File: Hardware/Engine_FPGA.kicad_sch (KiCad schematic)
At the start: 8 parts, among them J12 Conn_02x05_Odd_Even, SW1 SW_KJ06RTT, U2 AT40K20-2EQJ

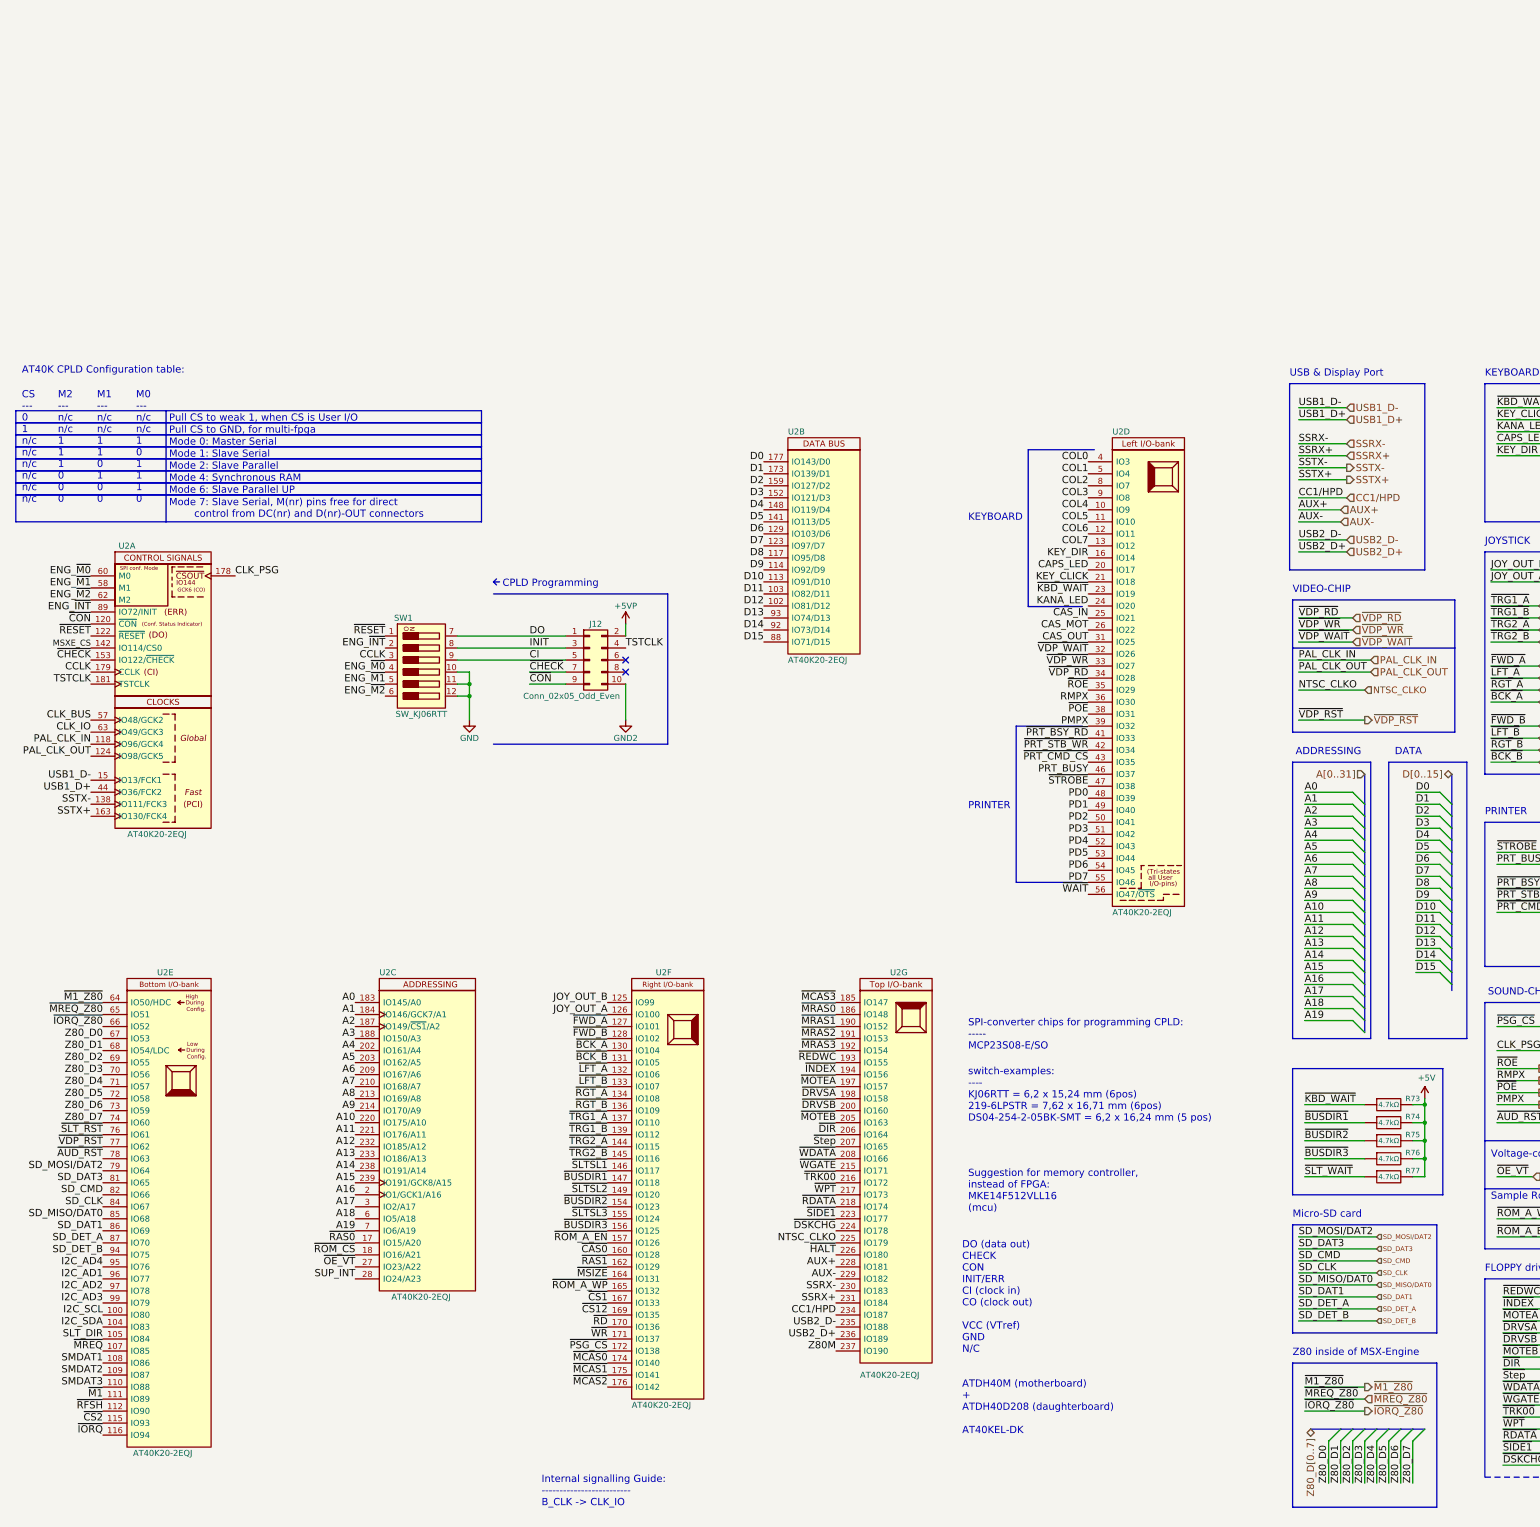
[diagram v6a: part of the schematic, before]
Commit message: Multiple redesigns of the IO-shield. Replaced FPGA with lower pin-count AT10K, since the higher pin-count one is now obsolete.
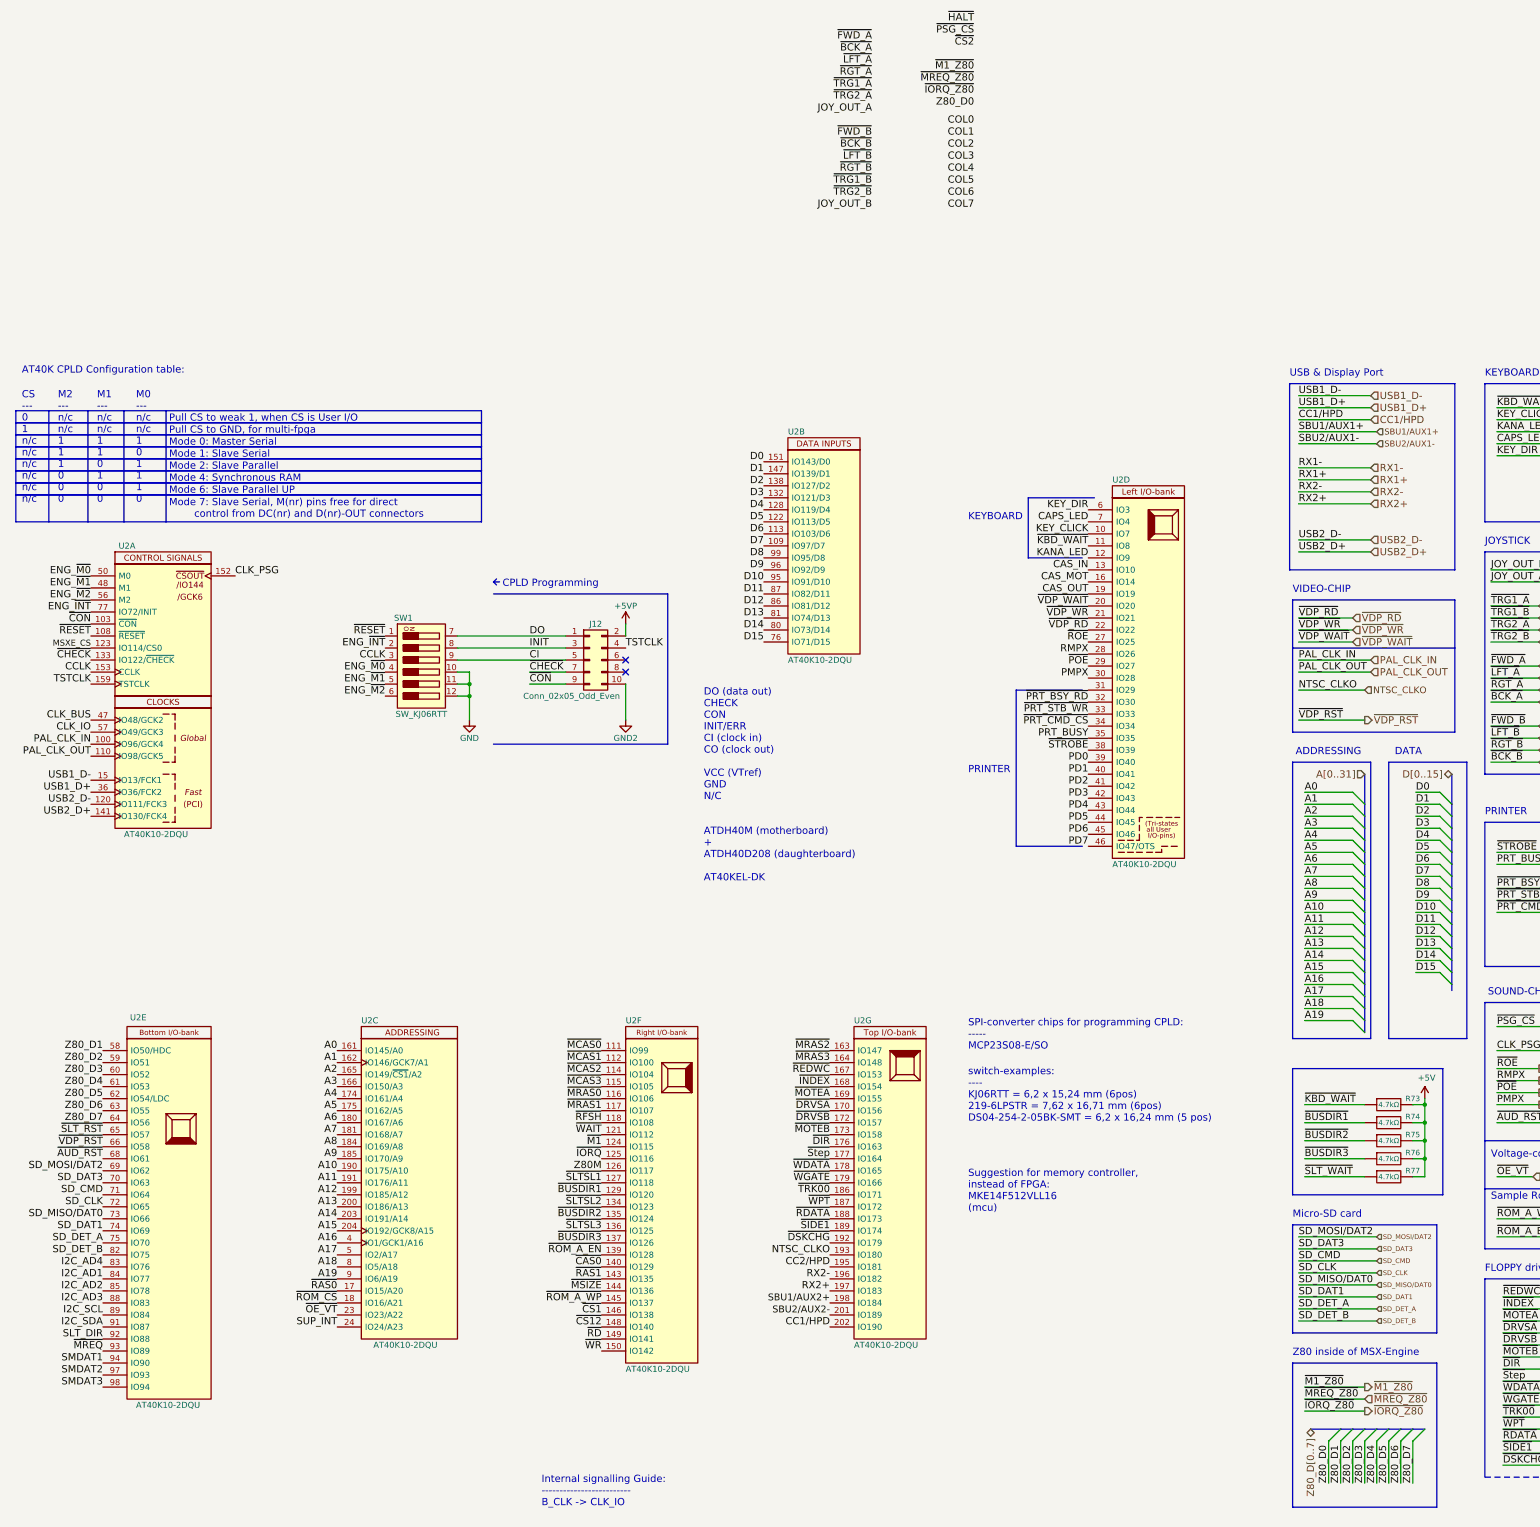
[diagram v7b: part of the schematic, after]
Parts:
- U2: value AT40K20-2EQJ -> AT40K10-2DQU; footprint Package_QFP:PQFP-240_32.1x32.1mm_P0.5mm -> Package_QFP:PQFP-208_28x28mm_P0.5mm; symbol LRJ-parts:AT40K20-2EQJ -> LRJ-parts:AT40K10-2DQU; MPN AT40K20-2EQJ -> AT40K10-2DQU; Manufacturer (none) -> Microchip/ATmel; Manufacturer_Name Microchip -> (none); Status (none) -> Active
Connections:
- net A0: now also U2.161 (IO145/A0); no longer U2.183 (IO145/A0)
- net A1: now also U2.162 (IO146/GCK7/A1); no longer U2.184 (IO146/GCK7/A1)
- net A10: now also U2.190 (IO175/A10); no longer U2.220 (IO175/A10)
- net A11: now also U2.191 (IO176/A11); no longer U2.221 (IO176/A11)
- net A12: now also U2.199 (IO185/A12); no longer U2.232 (IO185/A12)
- net A13: now also U2.200 (IO186/A13); no longer U2.233 (IO186/A13)
- net A14: now also U2.203 (IO191/A14); no longer U2.238 (IO191/A14)
- net A15: now also U2.204 (IO192/GCK8/A15); no longer U2.239 (IO191/GCK8/A15)
- net A16: now also U2.4 (IO1/GCK1/A16); no longer U2.2 (IO1/GCK1/A16)
- net A17: now also U2.5 (IO2/A17); no longer U2.3 (IO2/A17)
- net A18: now also U2.8 (IO5/A18); no longer U2.6 (IO5/A18)
- net A19: now also U2.9 (IO6/A19); no longer U2.7 (IO6/A19)
- net A2: now also U2.165 (IO149/~{CS1}/A2); no longer U2.187 (IO149/~{CS1}/A2)
- net A3: now also U2.166 (IO150/A3); no longer U2.188 (IO150/A3)
- net A4: now also U2.174 (IO161/A4); no longer U2.202 (IO161/A4)
- net A5: now also U2.175 (IO162/A5); no longer U2.203 (IO162/A5)
- net A6: now also U2.180 (IO167/A6); no longer U2.209 (IO167/A6)
- net A7: now also U2.181 (IO168/A7); no longer U2.210 (IO168/A7)
- net A8: now also U2.184 (IO169/A8); no longer U2.213 (IO169/A8)
- net A9: now also U2.185 (IO170/A9); no longer U2.214 (IO170/A9)
- net CAPS_LED: now also U2.7 (IO4); no longer U2.20 (IO17)
- net CAS_IN: now also U2.13 (IO10); no longer U2.25 (IO21)
- net CAS_MOT: now also U2.16 (IO14); no longer U2.26 (IO22)
- net CAS_OUT: now also U2.19 (IO19); no longer U2.31 (IO25)
- net CC1/HPD: now also U2.202 (IO190); no longer U2.234 (IO187)
- net CCLK: now also U2.153 (CCLK); no longer U2.179 (CCLK)
- net CLK_BUS: now also U2.47 (IO48/GCK2); no longer U2.57 (IO48/GCK2)
- net CLK_IO: now also U2.57 (IO49/GCK3); no longer U2.63 (IO49/GCK3)
- net CLK_PSG: now also U2.152 (IO144/GCK6/~{CSOUT}); no longer U2.178 (IO144/GCK6/~{CSOUT})
- net COL0: no longer U2.4 (IO3)
- net COL1: no longer U2.5 (IO4)
- net COL2: no longer U2.8 (IO7)
- net COL3: no longer U2.9 (IO8)
- net COL4: no longer U2.10 (IO9)
- net COL5: no longer U2.11 (IO10)
- net COL6: no longer U2.12 (IO11)
- net COL7: no longer U2.13 (IO12)
- net D0: now also U2.151 (IO143/D0); no longer U2.177 (IO143/D0)
- net D1: now also U2.147 (IO139/D1); no longer U2.173 (IO139/D1)
- net D10: now also U2.95 (IO91/D10); no longer U2.113 (IO91/D10)
- net D11: now also U2.87 (IO82/D11); no longer U2.103 (IO82/D11)
- net D12: now also U2.86 (IO81/D12); no longer U2.102 (IO81/D12)
- net D13: now also U2.81 (IO74/D13); no longer U2.93 (IO74/D13)
- net D14: now also U2.80 (IO73/D14); no longer U2.92 (IO73/D14)
- net D15: now also U2.76 (IO71/D15); no longer U2.88 (IO71/D15)
- net D2: now also U2.138 (IO127/D2); no longer U2.159 (IO127/D2)
- net D3: now also U2.132 (IO121/D3); no longer U2.152 (IO121/D3)
- net D4: now also U2.128 (IO119/D4); no longer U2.148 (IO119/D4)
- net D5: now also U2.122 (IO113/D5); no longer U2.141 (IO113/D5)
- net D6: now also U2.113 (IO103/D6); no longer U2.129 (IO103/D6)
- net D7: now also U2.109 (IO97/D7); no longer U2.123 (IO97/D7)
- net D8: now also U2.99 (IO95/D8); no longer U2.117 (IO95/D8)
- net D9: now also U2.96 (IO92/D9); no longer U2.114 (IO92/D9)
- net ENG_~{INT}: now also U2.77 (IO72/INIT); no longer U2.89 (IO72/INIT)
- net ENG_~{M0}: now also U2.50 (M0); no longer U2.60 (M0)
- net ENG_~{M1}: now also U2.48 (M1); no longer U2.58 (M1)
- net ENG_~{M2}: now also U2.56 (M2); no longer U2.62 (M2)
- net I2C_AD1: now also U2.84 (IO77); no longer U2.96 (IO77)
- net I2C_AD2: now also U2.85 (IO78); no longer U2.97 (IO78)
- net I2C_AD3: now also U2.88 (IO83); no longer U2.99 (IO79)
- net I2C_AD4: now also U2.83 (IO76); no longer U2.95 (IO76)
- net I2C_SCL: now also U2.89 (IO84); no longer U2.100 (IO80)
- net I2C_SDA: now also U2.91 (IO87); no longer U2.104 (IO83)
- net JOY_OUT_A: no longer U2.126 (IO100)
- net JOY_OUT_B: no longer U2.125 (IO99)
- net KANA_LED: now also U2.12 (IO9); no longer U2.24 (IO20)
- net KEY_CLICK: now also U2.10 (IO7); no longer U2.21 (IO18)
- net KEY_DIR: now also U2.6 (IO3); no longer U2.16 (IO14)
- net MSXE_CS: now also U2.123 (IO114/CS0); no longer U2.142 (IO114/CS0)
- net NTSC_CLKO: now also U2.193 (IO180); no longer U2.225 (IO179)
- net PAL_CLK_IN: now also U2.100 (IO96/GCK4); no longer U2.118 (IO96/GCK4)
- net PAL_CLK_OUT: now also U2.110 (IO98/GCK5); no longer U2.124 (IO98/GCK5)
- net PD0: now also U2.39 (IO40); no longer U2.48 (IO39)
- net PD1: now also U2.40 (IO41); no longer U2.49 (IO40)
- net PD2: now also U2.41 (IO42); no longer U2.50 (IO41)
- net PD3: now also U2.42 (IO43); no longer U2.51 (IO42)
- net PD4: now also U2.43 (IO44); no longer U2.52 (IO43)
- net PD5: now also U2.44 (IO45); no longer U2.53 (IO44)
- net PD6: now also U2.45 (IO46); no longer U2.54 (IO45)
- net PD7: now also U2.46 (IO47/OTS); no longer U2.55 (IO46)
- net PMPX: now also U2.30 (IO28); no longer U2.39 (IO32)
- net PRT_BUSY: now also U2.35 (IO35); no longer U2.46 (IO37)
- net RMPX: now also U2.28 (IO26); no longer U2.36 (IO30)
- net SD_CLK: now also U2.72 (IO65); no longer U2.84 (IO67)
- net SD_CMD: now also U2.71 (IO64); no longer U2.82 (IO66)
- net SD_DAT1: now also U2.74 (IO69); no longer U2.86 (IO69)
- net SD_DAT3: now also U2.70 (IO63); no longer U2.81 (IO65)
- net SD_DET_A: now also U2.75 (IO70); no longer U2.87 (IO70)
- net SD_DET_B: now also U2.82 (IO75); no longer U2.94 (IO75)
- net SD_MISO/DAT0: now also U2.73 (IO66); no longer U2.85 (IO68)
- net SD_MOSI/DAT2: now also U2.69 (IO62); no longer U2.79 (IO64)
- net SLT_DIR: now also U2.92 (IO88); no longer U2.105 (IO84)
- net SMDAT1: now also U2.94 (IO90); no longer U2.108 (IO86)
- net SMDAT2: now also U2.97 (IO93); no longer U2.109 (IO87)
- net SMDAT3: now also U2.98 (IO94); no longer U2.110 (IO88)
- net SUP_INT: now also U2.24 (IO24/A23); no longer U2.28 (IO24/A23)
- net TSTCLK: now also U2.159 (TSTCLK); no longer U2.181 (TSTCLK)
- net USB1_D+: now also U2.36 (IO36/FCK2); no longer U2.44 (IO36/FCK2)
- net USB2_D+: now also U2.141 (IO130/FCK4); no longer U2.236 (IO189)
- net USB2_D-: now also U2.120 (IO111/FCK3); no longer U2.235 (IO188)
- net Z80M: now also U2.126 (IO117); no longer U2.237 (IO190)
- net Z80_D0: no longer U2.67 (IO53)
- net Z80_D1: now also U2.58 (IO50/HDC); no longer U2.68 (IO54/LDC)
- net Z80_D2: now also U2.59 (IO51); no longer U2.69 (IO55)
- net Z80_D3: now also U2.60 (IO52); no longer U2.70 (IO56)
- net Z80_D4: now also U2.61 (IO53); no longer U2.71 (IO57)
- net Z80_D5: now also U2.62 (IO54/LDC); no longer U2.72 (IO58)
- net Z80_D6: now also U2.63 (IO55); no longer U2.73 (IO59)
- net Z80_D7: now also U2.64 (IO56); no longer U2.74 (IO60)
- net ~{AUD_RST}: now also U2.68 (IO61); no longer U2.78 (IO63)
- net ~{BCK_A}: no longer U2.130 (IO104)
- net ~{BCK_B}: no longer U2.131 (IO105)
- net ~{BUSDIR1}: now also U2.129 (IO120); no longer U2.147 (IO118)
- net ~{BUSDIR2}: now also U2.135 (IO124); no longer U2.154 (IO123)
- net ~{BUSDIR3}: now also U2.137 (IO126); no longer U2.156 (IO125)
- net ~{CAS0}: now also U2.140 (IO129); no longer U2.160 (IO128)
- net ~{CHECK}: now also U2.133 (IO122/~{CHECK}); no longer U2.153 (IO122/~{CHECK})
- net ~{CON}: now also U2.103 (~{CON}); no longer U2.120 (~{CON})
- net ~{CS12}: now also U2.148 (IO140); no longer U2.169 (IO135)
- net ~{CS1}: now also U2.146 (IO138); no longer U2.167 (IO133)
- net ~{CS2}: no longer U2.115 (IO93)
- net ~{DIR}: now also U2.176 (IO163); no longer U2.206 (IO164)
- net ~{DRVSA}: now also U2.170 (IO156); no longer U2.198 (IO158)
- net ~{DRVSB}: now also U2.172 (IO157); no longer U2.200 (IO160)
- net ~{DSKCHG}: now also U2.192 (IO179); no longer U2.224 (IO178)
- net ~{FWD_A}: no longer U2.127 (IO101)
- net ~{FWD_B}: no longer U2.128 (IO102)
- net ~{HALT}: no longer U2.226 (IO180)
- net ~{INDEX}: now also U2.168 (IO154); no longer U2.194 (IO156)
- net ~{IORQ_Z80}: no longer U2.66 (IO52)
- net ~{IORQ}: now also U2.125 (IO116); no longer U2.116 (IO94)
- net ~{KBD_WAIT}: now also U2.11 (IO8); no longer U2.23 (IO19)
- net ~{LFT_A}: no longer U2.132 (IO106)
- net ~{LFT_B}: no longer U2.133 (IO107)
- net ~{M1_Z80}: no longer U2.64 (IO50/HDC)
- net ~{M1}: now also U2.124 (IO115); no longer U2.111 (IO89)
- net ~{MCAS0}: now also U2.111 (IO99); no longer U2.174 (IO140)
- net ~{MCAS1}: now also U2.112 (IO100); no longer U2.175 (IO141)
- net ~{MCAS2}: now also U2.114 (IO104); no longer U2.176 (IO142)
- net ~{MCAS3}: now also U2.115 (IO105); no longer U2.185 (IO147)
- net ~{MOTEA}: now also U2.169 (IO155); no longer U2.197 (IO157)
- net ~{MOTEB}: now also U2.173 (IO158); no longer U2.205 (IO163)
- net ~{MRAS0}: now also U2.116 (IO106); no longer U2.186 (IO148)
- net ~{MRAS1}: now also U2.117 (IO107); no longer U2.190 (IO152)
- net ~{MRAS2}: now also U2.163 (IO147); no longer U2.191 (IO153)
- net ~{MRAS3}: now also U2.164 (IO148); no longer U2.192 (IO154)
- net ~{MREQ_Z80}: no longer U2.65 (IO51)
- net ~{MREQ}: now also U2.93 (IO89); no longer U2.107 (IO85)
- net ~{MSIZE}: now also U2.144 (IO136); no longer U2.164 (IO131)
- net ~{OE_VT}: now also U2.23 (IO23/A22); no longer U2.27 (IO23/A22)
- net ~{POE}: now also U2.29 (IO27); no longer U2.38 (IO31)
- net ~{PRT_BSY_RD}: now also U2.32 (IO30); no longer U2.41 (IO33)
- net ~{PRT_CMD_CS}: now also U2.34 (IO34); no longer U2.43 (IO35)
- net ~{PRT_STB_WR}: now also U2.33 (IO33); no longer U2.42 (IO34)
- net ~{PSG_CS}: no longer U2.172 (IO138)
- net ~{RAS1}: now also U2.143 (IO135); no longer U2.162 (IO129)
- net ~{RDATA}: now also U2.188 (IO173); no longer U2.218 (IO174)
- net ~{RD}: now also U2.149 (IO141); no longer U2.170 (IO136)
- net ~{REDWC}: now also U2.167 (IO153); no longer U2.193 (IO155)
- net ~{RESET}: now also U2.108 (~{RESET}); no longer U2.122 (~{RESET})
- net ~{RFSH}: now also U2.118 (IO108); no longer U2.112 (IO90)
- net ~{RGT_A}: no longer U2.134 (IO108)
- net ~{RGT_B}: no longer U2.136 (IO109)
- net ~{ROE}: now also U2.27 (IO25); no longer U2.35 (IO29)
- net ~{ROM_A_EN}: now also U2.139 (IO128); no longer U2.157 (IO126)
- net ~{ROM_A_WP}: now also U2.145 (IO137); no longer U2.165 (IO132)
- net ~{SIDE1}: now also U2.189 (IO174); no longer U2.223 (IO177)
- net ~{SLTSL1}: now also U2.127 (IO118); no longer U2.146 (IO117)
- net ~{SLTSL2}: now also U2.134 (IO123); no longer U2.149 (IO120)
- net ~{SLTSL3}: now also U2.136 (IO125); no longer U2.155 (IO124)
- net ~{SLT_RST}: now also U2.65 (IO57); no longer U2.76 (IO61)
- net ~{STROBE}: now also U2.38 (IO39); no longer U2.47 (IO38)
- net ~{Step}: now also U2.177 (IO164); no longer U2.207 (IO165)
- net ~{TRG1_A}: no longer U2.137 (IO110)
- net ~{TRG1_B}: no longer U2.139 (IO112)
- net ~{TRG2_A}: no longer U2.144 (IO115)
- net ~{TRG2_B}: no longer U2.145 (IO116)
- net ~{TRK00}: now also U2.186 (IO171); no longer U2.216 (IO172)
- net ~{VDP_RD}: now also U2.22 (IO22); no longer U2.34 (IO28)
- net ~{VDP_RST}: now also U2.66 (IO58); no longer U2.77 (IO62)
- net ~{VDP_WAIT}: now also U2.20 (IO20); no longer U2.32 (IO26)
- net ~{VDP_WR}: now also U2.21 (IO21); no longer U2.33 (IO27)
- net ~{WAIT}: now also U2.121 (IO112); no longer U2.56 (IO47/~{OTS})
- net ~{WDATA}: now also U2.178 (IO165); no longer U2.208 (IO166)
- net ~{WGATE}: now also U2.179 (IO166); no longer U2.215 (IO171)
- net ~{WPT}: now also U2.187 (IO172); no longer U2.217 (IO173)
- net ~{WR}: now also U2.150 (IO142); no longer U2.171 (IO137)
- removed net AUX+: U2.228 (IO181)
- removed net AUX-: U2.229 (IO182)
- removed net SSRX+: U2.231 (IO184)
- removed net SSRX-: U2.230 (IO183)
- removed net SSTX+: U2.163 (IO130/FCK4)
- removed net SSTX-: U2.138 (IO111/FCK3)
- new net CC2/HPD: U2.195 (IO181)
- new net RX2+: U2.197 (IO183)
- new net RX2-: U2.196 (IO182)
- new net SBU1/AUX2+: U2.198 (IO184)
- new net SBU2/AUX2-: U2.201 (IO189)

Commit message: Added cooler and CPU-mount footprints, as well as Indication LEDs.
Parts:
- added U16: AT40K10-2DQU, Package_QFP:PQFP-208_28x28mm_P0.5mm, symbol LRJ-parts:AT40K10-2DQU
- SW1: value SW_KJ06RTT -> SW_DS01-254; footprint LRJ:SW_DIP_DPSTx06_Slide_CIT_KJ06RTT_W6.2mm_P2.54mm -> LRJ:SW_DIP_DPSTx06_Slide_CUI_DS01_W9.9mm_P2.54mm; symbol LRJ-parts:SW_KJ06RTT -> LRJ-parts:SW_DS01-254; Height 4.1 mm -> (none); MPN (none) -> DS01-254-L-06BE; Manufacturer (none) -> CUI Devices; Manufacturer_Name CIT Relay and Switch -> (none); Manufacturer_Part_Number KJ06RTT -> (none)
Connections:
- net CC2/HPD is gone; now on net ~{RAS0}: U2.195 (IO181)
- net GND is gone; now on net +5VP: SW1.10, SW1.11, SW1.12
- net RX2+ is gone; now on net ~{OE_VT}: U2.197 (IO183)
- net RX2- is gone; now on net ~{ROM_CS}: U2.196 (IO182)
- net SBU1/AUX2+ is gone; now on net SUP_INT: U2.198 (IO184)
- net A17: now also U16.161 (IO145/A0)
- net A18: now also U16.162 (IO146/GCK7/A1)
- net A19: now also U16.165 (IO149/~{CS1}/A2)
- net CAPS_LED: now also U2.32 (IO30); no longer U2.7 (IO4)
- net CAS_IN: now also U2.6 (IO3); no longer U2.13 (IO10)
- net CAS_MOT: now also U2.7 (IO4); no longer U2.16 (IO14)
- net CAS_OUT: now also U2.10 (IO7); no longer U2.19 (IO19)
- net CC1/HPD: now also U16.17 (IO15/A20); no longer U2.202 (IO190)
- net CCLK: now also U16.153 (CCLK)
- net CLK_BUS: now also U2.57 (IO49/GCK3); no longer U2.47 (IO48/GCK2)
- net CLK_IO: now also U2.100 (IO96/GCK4); no longer U2.57 (IO49/GCK3)
- net COL0: now also U2.38 (IO39)
- net COL1: now also U2.39 (IO40)
- net COL2: now also U2.40 (IO41)
- net COL3: now also U2.41 (IO42)
- net COL4: now also U2.42 (IO43)
- net COL5: now also U2.43 (IO44)
- net COL6: now also U2.44 (IO45)
- net COL7: now also U2.45 (IO46)
- net D0: now also U16.151 (IO143/D0)
- net D1: now also U16.147 (IO139/D1)
- net D10: now also U16.95 (IO91/D10)
- net D11: now also U16.87 (IO82/D11)
- net D12: now also U16.86 (IO81/D12)
- net D13: now also U16.81 (IO74/D13)
- net D14: now also U16.80 (IO73/D14)
- net D15: now also U16.76 (IO71/D15)
- net D2: now also U16.138 (IO127/D2)
- net D3: now also U16.132 (IO121/D3)
- net D4: now also U16.128 (IO119/D4)
- net D5: now also U16.122 (IO113/D5)
- net D6: now also U16.113 (IO103/D6)
- net D7: now also U16.109 (IO97/D7)
- net D8: now also U16.99 (IO95/D8)
- net D9: now also U16.96 (IO92/D9)
- net I2C_AD1: now also U2.28 (IO26); no longer U2.84 (IO77)
- net I2C_AD2: now also U2.29 (IO27); no longer U2.85 (IO78)
- net I2C_AD3: now also U2.30 (IO28); no longer U2.88 (IO83)
- net I2C_AD4: now also U2.27 (IO25); no longer U2.83 (IO76)
- net INIT: now also U16.77 (IO72/INIT)
- net JOY_OUT_A: now also U16.64 (IO56)
- net JOY_OUT_B: now also U16.72 (IO65)
- net KANA_LED: now also U2.35 (IO35); no longer U2.12 (IO9)
- net KEY_CLICK: now also U2.33 (IO33); no longer U2.10 (IO7)
- net KEY_DIR: now also U2.31 (IO29); no longer U2.6 (IO3)
- net NTSC_CLKO: now also U2.141 (IO130/FCK4); no longer U2.193 (IO180)
- net PAL_CLK_IN: now also U2.110 (IO98/GCK5); no longer U2.100 (IO96/GCK4)
- net PAL_CLK_OUT: now also U2.36 (IO36/FCK2); no longer U2.110 (IO98/GCK5)
- net PD0: now also U16.73 (IO66); no longer U2.39 (IO40)
- net PD1: now also U16.74 (IO69); no longer U2.40 (IO41)
- net PD2: now also U16.75 (IO70); no longer U2.41 (IO42)
- net PD3: now also U16.82 (IO75); no longer U2.42 (IO43)
- net PD4: now also U16.83 (IO76); no longer U2.43 (IO44)
- net PD5: now also U16.84 (IO77); no longer U2.44 (IO45)
- net PD6: now also U16.85 (IO78); no longer U2.45 (IO46)
- net PD7: now also U16.88 (IO83); no longer U2.46 (IO47/OTS)
- net PMPX: now also U2.21 (IO21); no longer U2.30 (IO28)
- net PRT_BUSY: now also U16.93 (IO89); no longer U2.35 (IO35)
- net RMPX: now also U2.19 (IO19); no longer U2.28 (IO26)
- net SD_CLK: now also U2.85 (IO78); no longer U2.72 (IO65)
- net SD_CMD: now also U2.84 (IO77); no longer U2.71 (IO64)
- net SD_DAT1: now also U2.75 (IO70); no longer U2.74 (IO69)
- net SD_DAT3: now also U2.83 (IO76); no longer U2.70 (IO63)
- net SD_DET_A: now also U2.61 (IO53); no longer U2.75 (IO70)
- net SD_DET_B: now also U2.62 (IO54/LDC); no longer U2.82 (IO75)
- net SD_MISO/DAT0: now also U2.88 (IO83); no longer U2.73 (IO66)
- net SD_MOSI/DAT2: now also U2.82 (IO75); no longer U2.69 (IO62)
- net SUP_INT: no longer U2.24 (IO24/A23)
- net TSTCLK: now also U16.159 (TSTCLK)
- net USB1_D+: now also U16.110 (IO98/GCK5); no longer U2.36 (IO36/FCK2)
- net USB1_D-: now also U16.100 (IO96/GCK4); no longer U2.15 (IO13/FCK1)
- net USB2_D+: now also U16.141 (IO130/FCK4); no longer U2.141 (IO130/FCK4)
- net USB2_D-: now also U16.120 (IO111/FCK3); no longer U2.120 (IO111/FCK3)
- net Z80_D0: now also U2.66 (IO58)
- net Z80_D1: now also U2.68 (IO61); no longer U2.58 (IO50/HDC)
- net Z80_D2: now also U2.69 (IO62); no longer U2.59 (IO51)
- net Z80_D3: now also U2.70 (IO63); no longer U2.60 (IO52)
- net Z80_D4: now also U2.71 (IO64); no longer U2.61 (IO53)
- net Z80_D5: now also U2.72 (IO65); no longer U2.62 (IO54/LDC)
- net Z80_D6: now also U2.73 (IO66); no longer U2.63 (IO55)
- net Z80_D7: now also U2.74 (IO69); no longer U2.64 (IO56)
- net ~{AUD_RST}: now also U2.60 (IO52); no longer U2.68 (IO61)
- net ~{BCK_A}: now also U16.59 (IO51)
- net ~{BCK_B}: now also U16.66 (IO58)
- net ~{CHECK}: now also U16.133 (IO122/~{CHECK})
- net ~{CON}: now also U16.103 (~{CON})
- net ~{CS2}: now also U2.193 (IO180)
- net ~{FWD_A}: now also U16.58 (IO50/HDC)
- net ~{FWD_B}: now also U16.65 (IO57)
- net ~{HALT}: now also U2.22 (IO22)
- net ~{IORQ_Z80}: now also U2.65 (IO57)
- net ~{KBD_WAIT}: now also U2.34 (IO34); no longer U2.11 (IO8)
- net ~{LFT_A}: now also U16.60 (IO52)
- net ~{LFT_B}: now also U16.68 (IO61)
- net ~{M1_Z80}: now also U2.63 (IO55)
- net ~{MREQ_Z80}: now also U2.64 (IO56)
- net ~{OE_VT}: no longer U2.23 (IO23/A22)
- net ~{POE}: now also U2.20 (IO20); no longer U2.29 (IO27)
- net ~{PRT_BSY_RD}: now also U16.89 (IO84); no longer U2.32 (IO30)
- net ~{PRT_CMD_CS}: now also U16.92 (IO88); no longer U2.34 (IO34)
- net ~{PRT_STB_WR}: now also U16.91 (IO87); no longer U2.33 (IO33)
- net ~{PSG_CS}: now also U2.46 (IO47/OTS)
- net ~{RAS0}: no longer U2.17 (IO15/A20)
- net ~{RD}: now also U16.123 (IO114/CS0)
- net ~{RESET}: now also U16.108 (~{RESET})
- net ~{RGT_A}: now also U16.61 (IO53)
- net ~{RGT_B}: now also U16.69 (IO62)
- net ~{ROE}: now also U2.16 (IO14); no longer U2.27 (IO25)
- net ~{ROM_CS}: no longer U2.18 (IO16/A21)
- net ~{SLT_RST}: now also U2.58 (IO50/HDC); no longer U2.65 (IO57)
- net ~{STROBE}: now also U16.94 (IO90); no longer U2.38 (IO39)
- net ~{TRG1_A}: now also U16.62 (IO54/LDC)
- net ~{TRG1_B}: now also U16.70 (IO63)
- net ~{TRG2_A}: now also U16.63 (IO55)
- net ~{TRG2_B}: now also U16.71 (IO64)
- net ~{VDP_RD}: now also U2.13 (IO10); no longer U2.22 (IO22)
- net ~{VDP_RST}: now also U2.59 (IO51); no longer U2.66 (IO58)
- net ~{VDP_WAIT}: now also U2.11 (IO8); no longer U2.20 (IO20)
- net ~{VDP_WR}: now also U2.12 (IO9); no longer U2.21 (IO21)
- net ~{WR}: now also U16.204 (IO192/GCK8/A15)
- net ENG_~{M0} renamed ENG_M0
- net ENG_M0: now also U16.50 (M0)
- net ENG_~{M1} renamed ENG_M1
- net ENG_M1: now also U16.48 (M1)
- net ENG_~{M2} renamed ENG_M2
- net ENG_M2: now also U16.56 (M2)
- net SBU2/AUX2-: no longer names the net of U2.201 (IO189)
- new net A20: U16.166 (IO150/A3), U2.17 (IO15/A20)
- new net A21: U16.174 (IO161/A4), U2.18 (IO16/A21)
- new net A22: U16.175 (IO162/A5), U2.23 (IO23/A22)
- new net A23: U16.180 (IO167/A6), U2.24 (IO24/A23)
- new net A24: U16.181 (IO168/A7)
- new net A25: U16.184 (IO169/A8)
- new net A26: U16.185 (IO170/A9)
- new net A27: U16.190 (IO175/A10)
- new net A28: U16.191 (IO176/A11)
- new net A29: U16.199 (IO185/A12)
- new net A30: U16.200 (IO186/A13)
- new net A31: U16.203 (IO191/A14)
- new net CLK_VDP: U2.120 (IO111/FCK3)
- new net MD0: U16.18 (IO16/A21)
- new net MD1: U16.23 (IO23/A22)
- new net MD10: U16.19 (IO19)
- new net MD11: U16.20 (IO20)
- new net MD12: U16.21 (IO21)
- new net MD13: U16.22 (IO22)
- new net MD14: U16.27 (IO25)
- new net MD15: U16.28 (IO26)
- new net MD16: U16.29 (IO27)
- new net MD17: U16.30 (IO28)
- new net MD18: U16.31 (IO29)
- new net MD19: U16.32 (IO30)
- new net MD2: U16.24 (IO24/A23)
- new net MD20: U16.33 (IO33)
- new net MD21: U16.34 (IO34)
- new net MD22: U16.35 (IO35)
- new net MD23: U16.38 (IO39)
- new net MD24: U16.39 (IO40)
- new net MD25: U16.40 (IO41)
- new net MD26: U16.41 (IO42)
- new net MD27: U16.42 (IO43)
- new net MD28: U16.43 (IO44)
- new net MD29: U16.44 (IO45)
- new net MD3: U16.6 (IO3)
- new net MD30: U16.45 (IO46)
- new net MD31: U16.46 (IO47/OTS)
- new net MD4: U16.7 (IO4)
- new net MD5: U16.10 (IO7)
- new net MD6: U16.11 (IO8)
- new net MD7: U16.12 (IO9)
- new net MD8: U16.13 (IO10)
- new net MD9: U16.16 (IO14)
- new net SWDCLK/RX1-: U16.8 (IO5/A18)
- new net SWDIO/RX1+: U16.4 (IO1/GCK1/A16)
- new net SWO/RX2-: U16.9 (IO6/A19)
- new net nRESET/RX2+: U16.5 (IO2/A17)
- no-connect marks 2 -> 63
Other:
- note added: "AT40K FPGA Configuration table:"
- note added: "CSOUT(clk_psg)"
- note added: "DO (data out) CHECK CON INIT/ERR CI (clock in) CO (clock out) VCC (VTref) GND N/C"
- note added: "FPGA Programming"
- note added: "Internal Z80"
- note added: "JOYSTICKS"
- note added: "MSX-engine chips: ------------ PPI ---- v- 7400 (four 2-input NAND) v- 7430 (x2) (8-input NAND) v- 7432 (x3) (four 2-input OR) v- 74273 (x2) (eight D-type flip-flop with reset; positive-edge trigger) -74540 (Octal buffer/line driver; inverting) -74541 (x3) (8-bit Buffer/Line Driver) v- 74153 (x2) (two 4-input multiplexer) v- 8255 Logic: 7x2 NAND + 4 NAND (18 NAND) 4x3 OR (36 NAND) 8x2 Flip-flop (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"
- note added: "Optional:"
- note added: "SPI-converter chips for programming FPGA: ----- MCP23S08-E/SO"
- note added: "USB-JTAG: --------- RX1- = SWDCLK RX1+ = SWDIO RX2- = SWO RX2+ = nReSeT SBU1 = VCC(target) SBU2 = GND"
- note added: "~{CHECK}"
- note removed: "AT40K CPLD Configuration table:"
- note removed: "CPLD Programming"
- note removed: "DO (data out) CHECK CON INIT/ERR CI (clock in) CO (clock out) VCC (VTref) GND N/C ATDH40M (motherboard) + ATDH40D208 (daughterboard) AT40KEL-DK"
- note removed: "Internal signalling Guide: ------------------------- B_CLK -> CLK_IO"
- note removed: "SPI-converter chips for programming CPLD: ----- MCP23S08-E/SO"
- note removed: "Suggestion for memory controller, instead of FPGA: MKE14F512VLL16 (mcu)"
- moved on the sheet: J12, SW1, U2B, U2C, U2D, U2E, U2F, U2G
